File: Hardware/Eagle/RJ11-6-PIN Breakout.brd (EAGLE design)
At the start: 17.8 x 20.6 mm, 2 parts, among them J1 Molex 22122044, J2 Amphenol MRJR-3460-0F

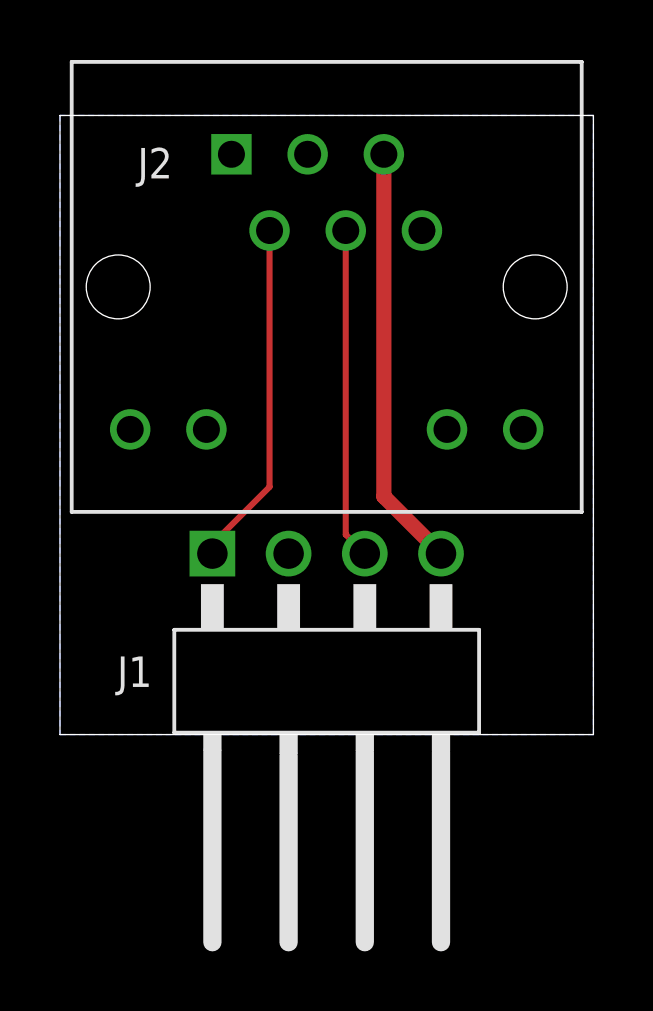
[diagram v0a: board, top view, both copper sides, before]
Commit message: Re-pinned the serial connector, changed track widths
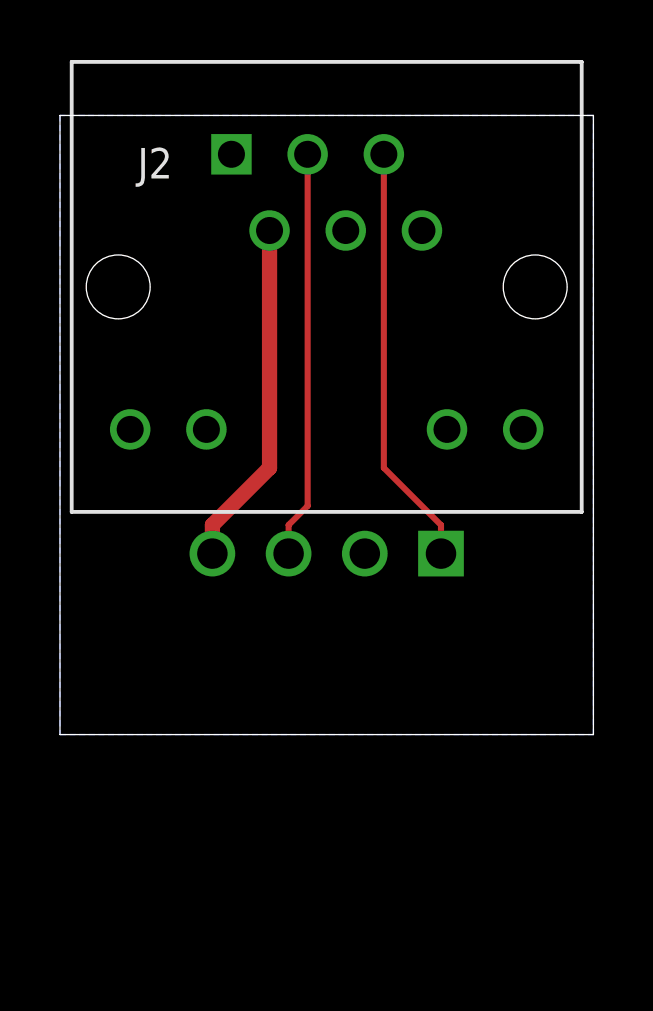
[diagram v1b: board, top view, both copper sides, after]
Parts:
- moved J1 2.54 mm to (7.62, 2.22), flipped to the bottom
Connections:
- net GND: now also J2.4; no longer J2.3
- net RX: now also J2.3; no longer J2.4
- net TX: now also J2.5; no longer J2.2
- net VCC: now also J2.2; no longer J2.5
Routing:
- net VCC: track 14.1 -> 11.6 mm
- net TX: track 11.6 -> 14.1 mm
- net RX: track 11.0 -> 13.6 mm
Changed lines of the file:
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@@
 <setting verticaltext="up"/>
 </settings>
-<grid distance="0.025" unitdist="inch" unit="inch" style="lines" multiple="1" display="yes" altdistance="5" altunitdist="mil" altunit="mil"/>
+<grid distance="0.0125" unitdist="inch" unit="inch" style="lines" multiple="1" display="yes" altdistance="5" altunitdist="mil" altunit="mil"/>
 <layers>
 <layer number="1" name="Top" color="4" fill="1" visible="yes" active="yes"/>
@@
 </layers>
 <board>
-<fusionsync huburn="a.cGVyc29uYWw6dWUyZDgyNjcx" projecturn="a.cGVyc29uYWw6dWUyZDgyNjcxIzIwMTgxMjIwMTY2NDc1MjMx" f3durn="urn:adsk.wipprod:dm.lineage:SILO-arIReG6jrEVXBfZUQ" pcbguid="" lastpulledtime="" lastsyncedchangeguid="" latestrevisionid="29585204-a2a1-4612-8995-8d23753b975b" lastsyncedrevisionid="29585204-a2a1-4612-8995-8d23753b975b" lastboardhashguid="4d23337f-3755-2952-6923-9db0f8f3c9bc" lastpushedtime="2020-11-29T18:58:21Z" linktopcb3d="true"/>
+<fusionsync huburn="a.cGVyc29uYWw6dWUyZDgyNjcx" projecturn="a.cGVyc29uYWw6dWUyZDgyNjcxIzIwMTgxMjIwMTY2NDc1MjMx" f3durn="urn:adsk.wipprod:dm.lineage:SILO-arIReG6jrEVXBfZUQ" pcbguid="" lastpulledtime="" lastsyncedchangeguid="" latestrevisionid="04bb935f-2475-484b-8848-9b20a462b751" lastsyncedrevisionid="04bb935f-2475-484b-8848-9b20a462b751" lastboardhashguid="8e97e618-9e73-e546-d7d0-0b72a1b0db5e" lastpushedtime="2021-02-19T15:52:04Z" linktopcb3d="true"/>
 <plain>
 <wire x1="0" y1="0" x2="17.78" y2="0" width="0" layer="20"/>
@@
 <wire x1="17.78" y1="20.6375" x2="0" y2="20.6375" width="0" layer="20"/>
 <wire x1="0" y1="20.6375" x2="0" y2="0" width="0" layer="20"/>
-<text x="14.605" y="6.0325" size="1.016" layer="22" rot="MR180">+5V</text>
-<text x="10.795" y="11.1125" size="1.016" layer="22" rot="MR270">RX</text>
-<text x="8.255" y="11.7475" size="1.016" layer="22" rot="MR270">GND</text>
-<text x="1.905" y="6.0325" size="1.016" layer="22" rot="MR180">TX</text>
+<text x="15.875" y="5.3975" size="1.016" layer="22" rot="MR0">TX</text>
+<text x="9.525" y="7.9375" size="1.016" layer="22" rot="MR90">GND</text>
+<text x="6.985" y="7.9375" size="1.016" layer="22" rot="MR90">RX</text>
+<text x="3.81" y="5.3975" size="1.016" layer="22" rot="MR0">+5V</text>
 </plain>
 <attributes>
@@
 <attribute name="NAME" x="2.585" y="18.5375" size="1.016" layer="25"/>
 </element>
-<element name="J1" library="AUmlib" library_urn="urn:adsk.eagle:library:9166017" package="1X04RA-MOLEX-22122044" package3d_urn="urn:adsk.eagle:package:25075311/2" value="Molex 22122044" x="10.16" y="2.2225" smashed="yes">
-<attribute name="NAME" x="1.905" y="1.5875" size="1.016" layer="25" font="vector"/>
+<element name="J1" library="AUmlib" library_urn="urn:adsk.eagle:library:9166017" package="1X04RA-MOLEX-22122044" package3d_urn="urn:adsk.eagle:package:25075311/2" value="Molex 22122044" x="7.62" y="2.2225" smashed="yes" rot="MR0">
+<attribute name="NAME" x="15.875" y="1.5875" size="1.016" layer="26" font="vector" rot="MR0"/>
 </element>
 </elements>
 <signals>
-<signal name="TX">
-<contactref element="J2" pad="2"/>
-<contactref element="J1" pad="1"/>
-<wire x1="6.985" y1="16.8025" x2="6.985" y2="8.255" width="0.2032" layer="1"/>
-<wire x1="6.985" y1="8.255" x2="5.08" y2="6.35" width="0.2032" layer="1"/>
-<wire x1="5.08" y1="6.35" x2="5.08" y2="6.0325" width="0.1524" layer="1"/>
-</signal>
 <signal name="GND">
-<contactref element="J2" pad="3"/>
 <polygon width="0.1524" layer="16">
 <vertex x="0" y="0"/>
@@
 </polygon>
 <contactref element="J1" pad="2"/>
+<contactref element="J2" pad="4"/>
+</signal>
+<signal name="VCC">
+<contactref element="J1" pad="4"/>
+<contactref element="J2" pad="2"/>
+<wire x1="5.08" y1="6.0325" x2="5.08" y2="6.985" width="0.508" layer="1"/>
+<wire x1="5.08" y1="6.985" x2="6.985" y2="8.89" width="0.508" layer="1"/>
+<wire x1="6.985" y1="8.89" x2="6.985" y2="16.8025" width="0.508" layer="1"/>
 </signal>
 <signal name="RX">
-<contactref element="J2" pad="4"/>
+<contactref element="J2" pad="3"/>
 <contactref element="J1" pad="3"/>
-<wire x1="9.525" y1="16.8025" x2="9.525" y2="6.6675" width="0.2032" layer="1"/>
-<wire x1="9.525" y1="6.6675" x2="10.16" y2="6.0325" width="0.2032" layer="1"/>
+<wire x1="7.62" y1="6.0325" x2="7.62" y2="6.985" width="0.2032" layer="1"/>
+<wire x1="7.62" y1="6.985" x2="8.255" y2="7.62" width="0.2032" layer="1"/>
+<wire x1="8.255" y1="7.62" x2="8.255" y2="19.3425" width="0.2032" layer="1"/>
 </signal>
-<signal name="VCC">
+<signal name="TX">
 <contactref element="J2" pad="5"/>
-<contactref element="J1" pad="4"/>
-<wire x1="10.795" y1="7.9375" x2="12.7" y2="6.0325" width="0.508" layer="1"/>
-<wire x1="10.795" y1="19.3425" x2="10.795" y2="7.9375" width="0.508" layer="1"/>
+<contactref element="J1" pad="1"/>
+<wire x1="12.7" y1="6.0325" x2="12.7" y2="6.985" width="0.2032" layer="1"/>
+<wire x1="12.7" y1="6.985" x2="10.795" y2="8.89" width="0.2032" layer="1"/>
+<wire x1="10.795" y1="8.89" x2="10.795" y2="19.3425" width="0.2032" layer="1"/>
 </signal>
 </signals>
